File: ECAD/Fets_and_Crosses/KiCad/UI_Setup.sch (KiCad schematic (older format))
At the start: 15 parts, among them SW10 SW_DPDT_x2, SW11 SW_DPDT_x2, SW12 SW_Push

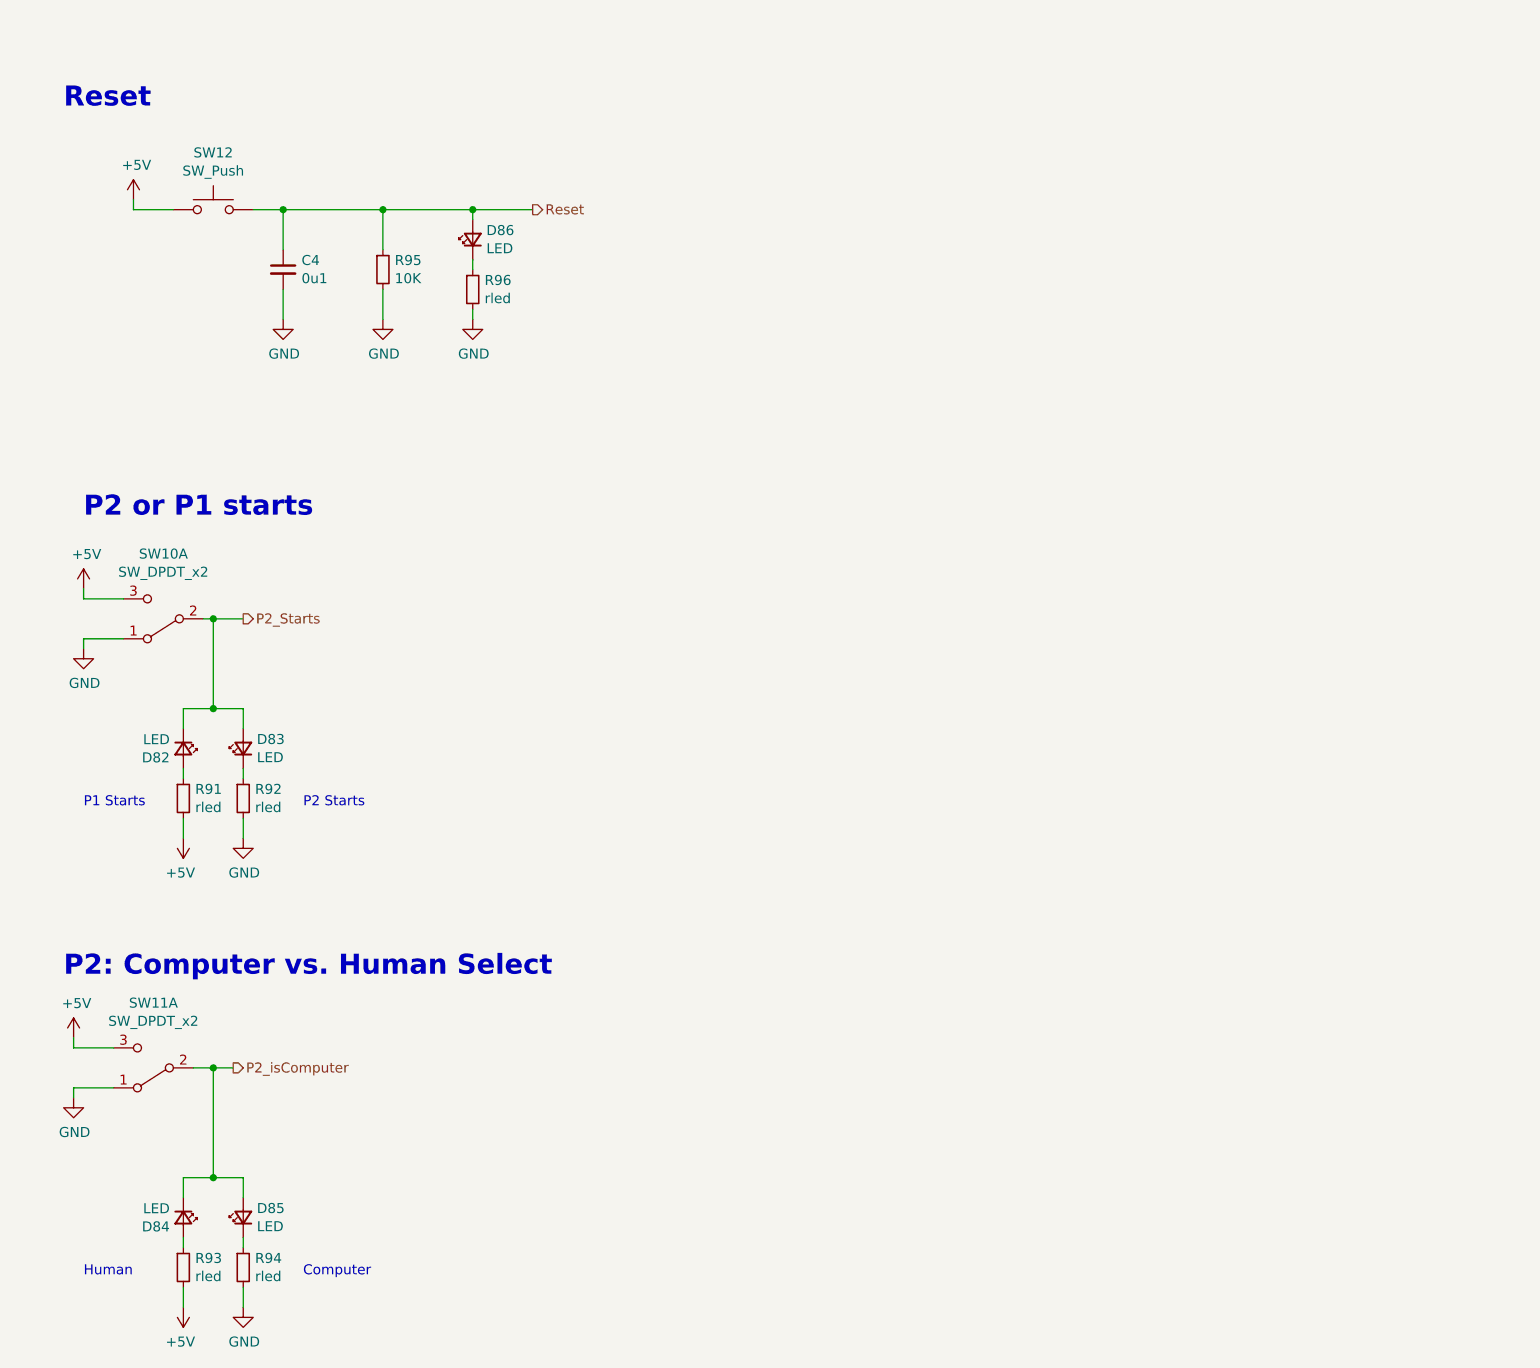
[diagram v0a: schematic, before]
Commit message: POR, Tooling Holes
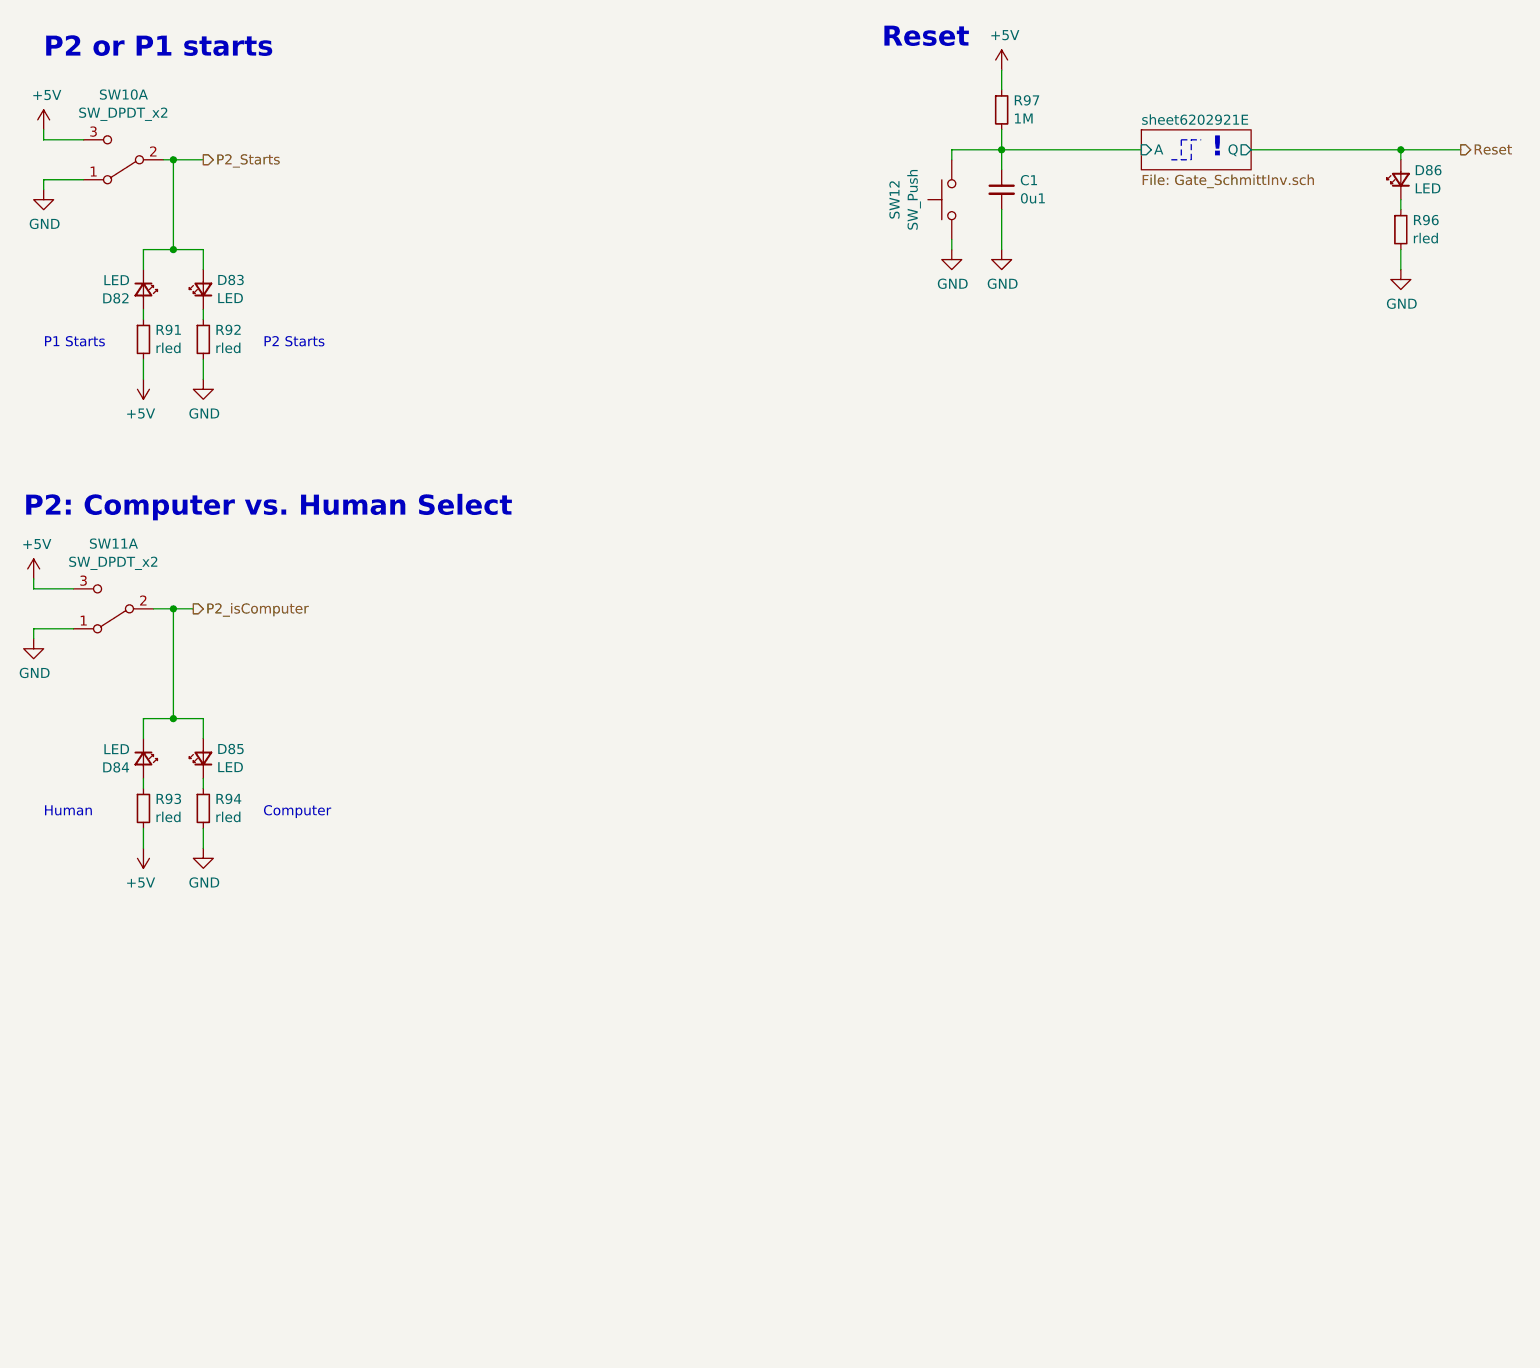
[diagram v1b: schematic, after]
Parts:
- removed C4: 0u1, LogicQ:C_0603_1608Metric_NOLBL, symbol Device:C_Small
- removed R95: 10K, Resistor_SMD:R_0603_1608Metric, symbol Device:R_Small
- added C1: 0u1, LogicQ:C_0603_1608Metric_NOLBL, symbol Device:C_Small
- added R97: 1M, Resistor_SMD:R_0603_1608Metric, symbol Device:R_Small
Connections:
- net +5V: now also R97.1; no longer SW12.1
- net GND: now also SW12.1, C1.2
- net Reset: no longer SW12.2
- new net sheet6202921E/A: C1.1, R97.2, SW12.2
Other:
- note added: "!"
- moved on the sheet: D82, D83, D84, D85, D86, R91, R92, R93, R94, R96, SW10A, SW11A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

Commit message: Seperated Red/Green LEDs
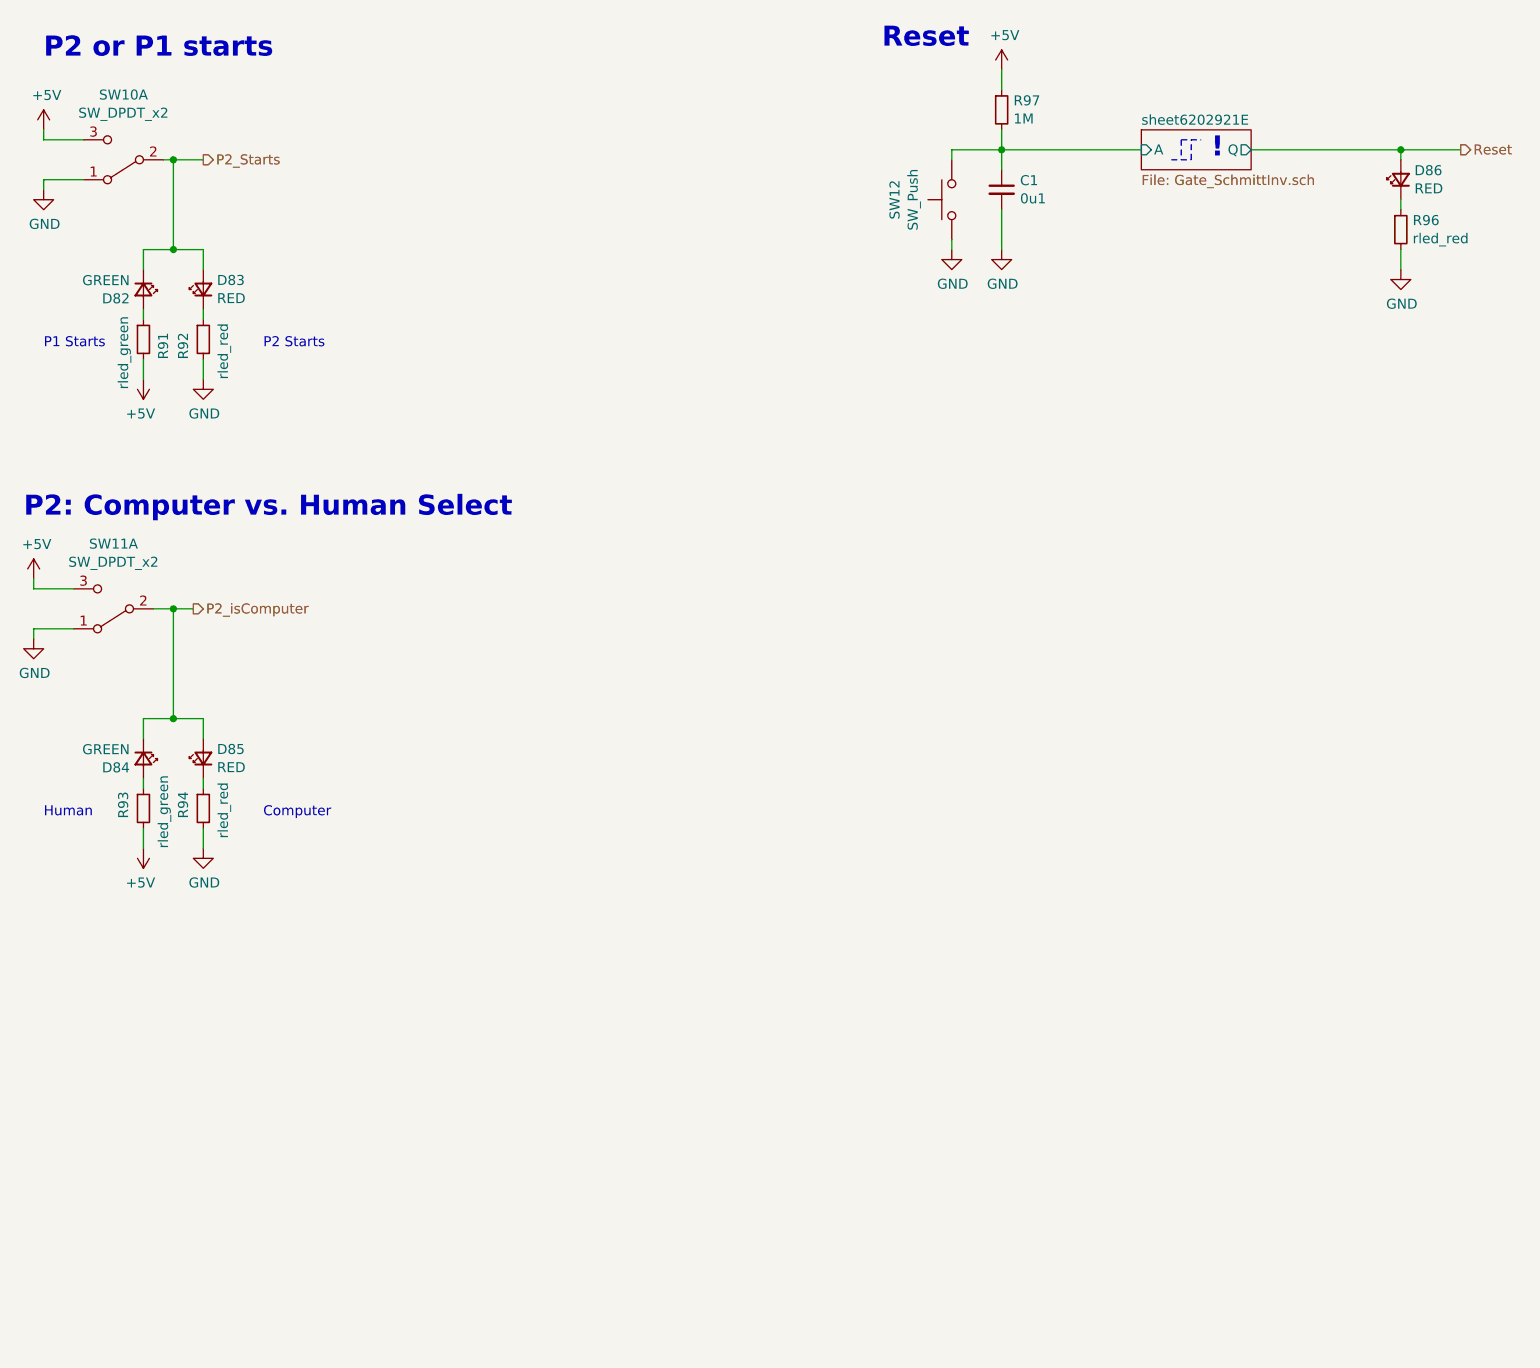
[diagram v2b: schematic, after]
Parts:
- D82, D84: value LED -> GREEN
- D83, D85, D86: value LED -> RED
- R91, R93: value rled -> rled_green
- R92, R94, R96: value rled -> rled_red
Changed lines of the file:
@@
 AR Path="/5E53AD22/5E6A228F/5F0CF22D" Ref="D82"  Part="1"
 F 0 "D82" V 2546 1932 50  0000 R CNN
-F 1 "LED" V 2455 1932 50  0000 R CNN
+F 1 "GREEN" V 2455 1932 50  0000 R CNN
 F 2 "LogicQ:D_0805_2012Metric_NOLBL" V 2500 2000 50  0001 C CNN
 F 3 "~" V 2500 2000 50  0001 C CNN
@@
 AR Path="/5E53AD22/5E56E949/5F0CF233" Ref="R?"  Part="1"
 AR Path="/5E53AD22/5E6A228F/5F0CF233" Ref="R91"  Part="1"
-F 0 "R91" H 2559 2296 50  0000 L CNN
-F 1 "rled" H 2559 2205 50  0000 L CNN
+F 0 "R91" V 2600 2150 50  0000 L CNN
+F 1 "rled_green" V 2400 2000 50  0000 L CNN
 F 2 "LogicQ:R_0603_1608Metric_NOLBL" H 2500 2250 50  0001 C CNN
 F 3 "~" H 2500 2250 50  0001 C CNN
@@
 AR Path="/5E53AD22/5E6A228F/5F0D1E29" Ref="D83"  Part="1"
 F 0 "D83" V 2846 1932 50  0000 R CNN
-F 1 "LED" V 2755 1932 50  0000 R CNN
+F 1 "RED" V 2755 1932 50  0000 R CNN
 F 2 "LogicQ:D_0805_2012Metric_NOLBL" V 2800 2000 50  0001 C CNN
 F 3 "~" V 2800 2000 50  0001 C CNN
@@
 AR Path="/5E53AD22/5E56E949/5F0D1E2F" Ref="R?"  Part="1"
 AR Path="/5E53AD22/5E6A228F/5F0D1E2F" Ref="R92"  Part="1"
-F 0 "R92" H 2859 2296 50  0000 L CNN
-F 1 "rled" H 2859 2205 50  0000 L CNN
+F 0 "R92" V 2700 2150 50  0000 L CNN
+F 1 "rled_red" V 2900 2050 50  0000 L CNN
 F 2 "LogicQ:R_0603_1608Metric_NOLBL" H 2800 2250 50  0001 C CNN
 F 3 "~" H 2800 2250 50  0001 C CNN
@@
 AR Path="/5E53AD22/5E6A228F/5F0D5BD6" Ref="D84"  Part="1"
 F 0 "D84" V 2546 4282 50  0000 R CNN
-F 1 "LED" V 2455 4282 50  0000 R CNN
+F 1 "GREEN" V 2455 4282 50  0000 R CNN
 F 2 "LogicQ:D_0805_2012Metric_NOLBL" V 2500 4350 50  0001 C CNN
 F 3 "~" V 2500 4350 50  0001 C CNN
@@
 AR Path="/5E53AD22/5E56E949/5F0D5BDC" Ref="R?"  Part="1"
 AR Path="/5E53AD22/5E6A228F/5F0D5BDC" Ref="R93"  Part="1"
-F 0 "R93" H 2559 4646 50  0000 L CNN
-F 1 "rled" H 2559 4555 50  0000 L CNN
+F 0 "R93" V 2400 4550 50  0000 L CNN
+F 1 "rled_green" V 2600 4400 50  0000 L CNN
 F 2 "LogicQ:R_0603_1608Metric_NOLBL" H 2500 4600 50  0001 C CNN
 F 3 "~" H 2500 4600 50  0001 C CNN
@@
 AR Path="/5E53AD22/5E6A228F/5F0D5BE4" Ref="D85"  Part="1"
 F 0 "D85" V 2846 4282 50  0000 R CNN
-F 1 "LED" V 2755 4282 50  0000 R CNN
+F 1 "RED" V 2755 4282 50  0000 R CNN
 F 2 "LogicQ:D_0805_2012Metric_NOLBL" V 2800 4350 50  0001 C CNN
 F 3 "~" V 2800 4350 50  0001 C CNN
@@
 AR Path="/5E53AD22/5E56E949/5F0D5BEA" Ref="R?"  Part="1"
 AR Path="/5E53AD22/5E6A228F/5F0D5BEA" Ref="R94"  Part="1"
-F 0 "R94" H 2859 4646 50  0000 L CNN
-F 1 "rled" H 2859 4555 50  0000 L CNN
+F 0 "R94" V 2700 4550 50  0000 L CNN
+F 1 "rled_red" V 2900 4450 50  0000 L CNN
 F 2 "LogicQ:R_0603_1608Metric_NOLBL" H 2800 4600 50  0001 C CNN
 F 3 "~" H 2800 4600 50  0001 C CNN
@@
 AR Path="/5E53AD22/5E6A228F/5F0F0600" Ref="D86"  Part="1"
 F 0 "D86" V 8846 1382 50  0000 R CNN
-F 1 "LED" V 8755 1382 50  0000 R CNN
+F 1 "RED" V 8755 1382 50  0000 R CNN
 F 2 "LogicQ:D_0805_2012Metric_NOLBL" V 8800 1450 50  0001 C CNN
 F 3 "~" V 8800 1450 50  0001 C CNN
@@
 AR Path="/5E53AD22/5E6A228F/5F0F0606" Ref="R96"  Part="1"
 F 0 "R96" H 8859 1746 50  0000 L CNN
-F 1 "rled" H 8859 1655 50  0000 L CNN
+F 1 "rled_red" H 8859 1655 50  0000 L CNN
 F 2 "LogicQ:R_0603_1608Metric_NOLBL" H 8800 1700 50  0001 C CNN
 F 3 "~" H 8800 1700 50  0001 C CNN

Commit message: Added Most LCSC Part Numbers
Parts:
- C1: LCSC (none) -> C14663
- D82, D84: LCSC (none) -> C84260
- D83, D85, D86: LCSC (none) -> C72037
- R97: LCSC (none) -> C22935
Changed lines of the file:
@@
 F 2 "LogicQ:D_0805_2012Metric_NOLBL" V 2500 2000 50  0001 C CNN
 F 3 "~" V 2500 2000 50  0001 C CNN
+F 4 "C84260" H 2500 2000 50  0001 C CNN "LCSC"
 	1    2500 2000
 	0    1    1    0
@@
 F 2 "LogicQ:D_0805_2012Metric_NOLBL" V 2800 2000 50  0001 C CNN
 F 3 "~" V 2800 2000 50  0001 C CNN
+F 4 "C72037" H 2800 2000 50  0001 C CNN "LCSC"
 	1    2800 2000
 	0    -1   -1   0
@@
 F 2 "LogicQ:D_0805_2012Metric_NOLBL" V 2500 4350 50  0001 C CNN
 F 3 "~" V 2500 4350 50  0001 C CNN
+F 4 "C84260" H 2500 4350 50  0001 C CNN "LCSC"
 	1    2500 4350
 	0    1    1    0
@@
 F 2 "LogicQ:D_0805_2012Metric_NOLBL" V 2800 4350 50  0001 C CNN
 F 3 "~" V 2800 4350 50  0001 C CNN
+F 4 "C72037" H 2800 4350 50  0001 C CNN "LCSC"
 	1    2800 4350
 	0    -1   -1   0
@@
 F 2 "LogicQ:D_0805_2012Metric_NOLBL" V 8800 1450 50  0001 C CNN
 F 3 "~" V 8800 1450 50  0001 C CNN
+F 4 "C72037" H 8800 1450 50  0001 C CNN "LCSC"
 	1    8800 1450
 	0    -1   -1   0
@@
 F 2 "Resistor_SMD:R_0603_1608Metric" H 6800 1100 50  0001 C CNN
 F 3 "~" H 6800 1100 50  0001 C CNN
+F 4 "C22935" H 6800 1100 50  0001 C CNN "LCSC"
 	1    6800 1100
 	1    0    0    -1
@@
 F 2 "LogicQ:C_0603_1608Metric_NOLBL" H 6800 1500 50  0001 C CNN
 F 3 "~" H 6800 1500 50  0001 C CNN
+F 4 "C14663" H 6800 1500 50  0001 C CNN "LCSC"
 	1    6800 1500
 	1    0    0    -1
